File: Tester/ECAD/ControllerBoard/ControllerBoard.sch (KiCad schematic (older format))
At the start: 5 parts, among them J1 Barrel_Jack, J2 Conn_01x02_Male, J3 Conn_01x02_Male, J4 Conn_01x02_Male, J5 Conn_01x02_Male

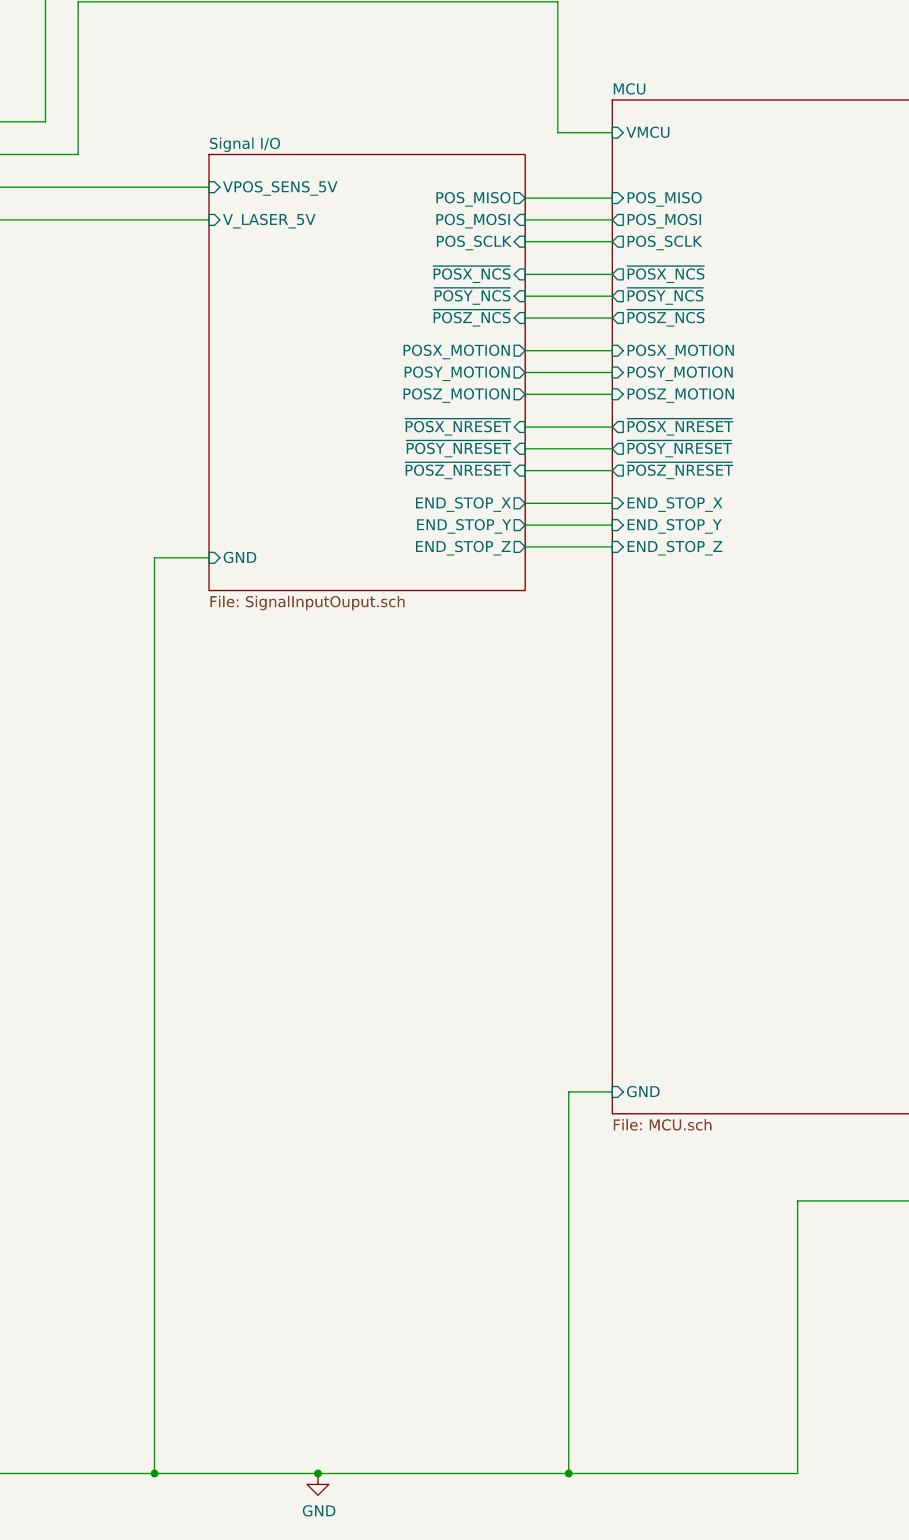
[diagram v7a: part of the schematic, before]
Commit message: Progressed circuit layout.
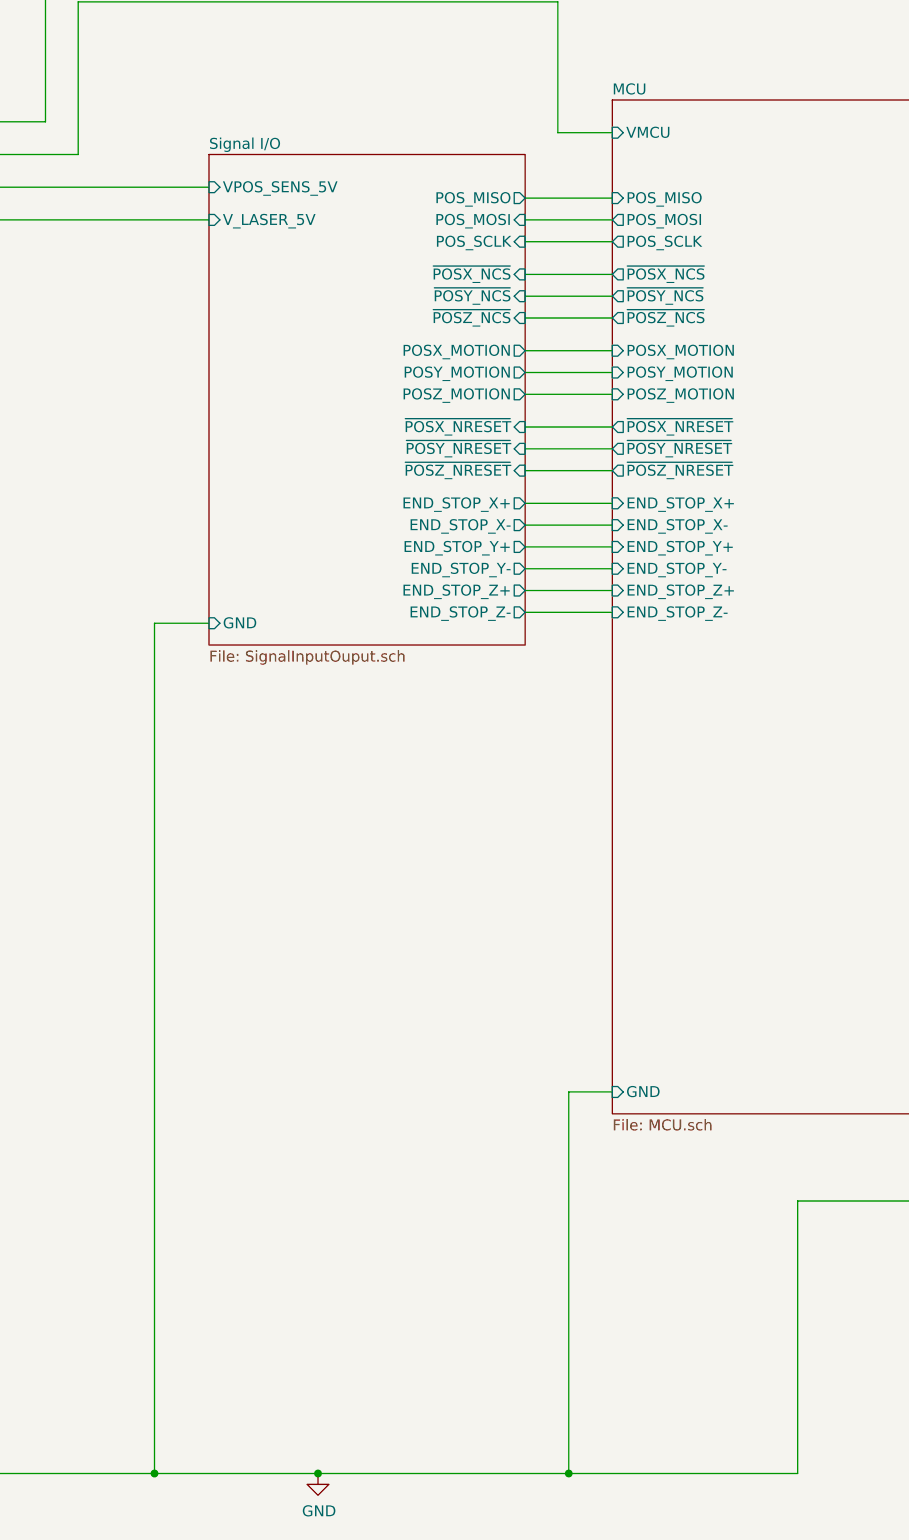
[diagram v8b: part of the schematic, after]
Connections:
- wire segments 59 -> 62
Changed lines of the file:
@@
 Wire Wire Line
 	3500 800  5700 800
-Wire Wire Line
-	1500 7550 3850 7550
 Connection ~ 4600 7550
 Connection ~ 5750 7550
@@
 F26 "~POSY_NRESET" O L 5950 2850 50
 F27 "~POSZ_NRESET" O L 5950 2950 50
-F28 "END_STOP_X" I L 5950 3100 50
-F29 "END_STOP_Y" I L 5950 3200 50
-F30 "END_STOP_Z" I L 5950 3300 50
+F28 "END_STOP_X+" I L 5950 3100 50
+F29 "END_STOP_Y+" I L 5950 3300 50
+F30 "END_STOP_Z+" I L 5950 3500 50
+F31 "END_STOP_X-" I L 5950 3200 50
+F32 "END_STOP_Y-" I L 5950 3400 50
+F33 "END_STOP_Z-" I L 5950 3600 50
 $EndSheet
 Wire Wire Line
@@
 Wire Wire Line
 	5950 2750 5550 2750
-Wire Wire Line
-	4100 3350 3850 3350
-Wire Wire Line
-	3850 3350 3850 7550
-Connection ~ 3850 7550
-Wire Wire Line
-	3850 7550 4600 7550
 $Sheet
-S 4100 1500 1450 2000
+S 4100 1500 1450 2250
 U 5E55806E
 F0 "Signal I/O" 50
@@
 F2 "V_LASER_5V" I L 4100 1800 50
 F3 "VPOS_SENS_5V" I L 4100 1650 50
-F4 "GND" I L 4100 3350 50
+F4 "GND" I L 4100 3650 50
 F5 "POS_MISO" O R 5550 1700 50
 F6 "POS_MOSI" I R 5550 1800 50
@@
 F15 "~POSY_NRESET" I R 5550 2850 50
 F16 "~POSZ_NRESET" I R 5550 2950 50
-F17 "END_STOP_X" O R 5550 3100 50
-F18 "END_STOP_Y" O R 5550 3200 50
-F19 "END_STOP_Z" O R 5550 3300 50
+F17 "END_STOP_X+" O R 5550 3100 50
+F18 "END_STOP_Y+" O R 5550 3300 50
+F19 "END_STOP_Z+" O R 5550 3500 50
+F20 "END_STOP_X-" O R 5550 3200 50
+F21 "END_STOP_Y-" O R 5550 3400 50
+F22 "END_STOP_Z-" O R 5550 3600 50
 $EndSheet
+Wire Wire Line
+	1500 7550 3850 7550
+Wire Wire Line
+	4100 3650 3850 3650
+Wire Wire Line
+	3850 3650 3850 7550
+Connection ~ 3850 7550
+Wire Wire Line
+	3850 7550 4600 7550
+Wire Wire Line
+	5950 3400 5550 3400
+Wire Wire Line
+	5550 3500 5950 3500
+Wire Wire Line
+	5950 3600 5550 3600
 $EndSCHEMATC
